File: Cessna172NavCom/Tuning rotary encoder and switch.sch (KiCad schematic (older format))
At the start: 7 parts, among them J3 EN11-HSM1BF20

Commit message: Mostly laid out
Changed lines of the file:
@@
 $Descr A4 11693 8268
 encoding utf-8
-Sheet 6 8
+Sheet 7 15
 Title ""
 Date ""
@@
 AR Path="/5F5DD336/5F5D9328" Ref="R9"  Part="1"
 AR Path="/5F5E0D77/5F5D9328" Ref="R13"  Part="1"
-F 0 "R9" V 5450 3850 50  0000 C CNN
+AR Path="/5F71BCE0/5F5D9328" Ref="R21"  Part="1"
+AR Path="/5F71BCEB/5F5D9328" Ref="R25"  Part="1"
+AR Path="/5F71BCF7/5F5D9328" Ref="R29"  Part="1"
+F 0 "R13" V 5450 3850 50  0000 C CNN
 F 1 "10k" V 5350 3850 50  0000 C CNN
 F 2 "Resistor_SMD:R_0805_2012Metric_Pad1.15x1.40mm_HandSolder" V 5180 3850 50  0001 C CNN
@@
 AR Path="/5F5DD336/5F5D932E" Ref="R10"  Part="1"
 AR Path="/5F5E0D77/5F5D932E" Ref="R14"  Part="1"
-F 0 "R10" V 5350 4050 50  0000 C CNN
+AR Path="/5F71BCE0/5F5D932E" Ref="R22"  Part="1"
+AR Path="/5F71BCEB/5F5D932E" Ref="R26"  Part="1"
+AR Path="/5F71BCF7/5F5D932E" Ref="R30"  Part="1"
+F 0 "R14" V 5350 4050 50  0000 C CNN
 F 1 "10k" V 5450 4050 50  0000 C CNN
 F 2 "Resistor_SMD:R_0805_2012Metric_Pad1.15x1.40mm_HandSolder" V 5180 4050 50  0001 C CNN
@@
 AR Path="/5F5DD336/5F5D9337" Ref="C9"  Part="1"
 AR Path="/5F5E0D77/5F5D9337" Ref="C11"  Part="1"
-F 0 "C9" V 6150 4750 50  0000 C CNN
+AR Path="/5F71BCE0/5F5D9337" Ref="C17"  Part="1"
+AR Path="/5F71BCEB/5F5D9337" Ref="C19"  Part="1"
+AR Path="/5F71BCF7/5F5D9337" Ref="C21"  Part="1"
+F 0 "C11" V 6150 4750 50  0000 C CNN
 F 1 "0.1uf" V 5850 4750 50  0000 C CNN
 F 2 "Capacitor_SMD:C_0805_2012Metric_Pad1.15x1.40mm_HandSolder" H 6038 4600 50  0001 C CNN
@@
 AR Path="/5F5DD336/5F5D933D" Ref="C8"  Part="1"
 AR Path="/5F5E0D77/5F5D933D" Ref="C10"  Part="1"
-F 0 "C8" V 5850 3050 50  0000 L CNN
+AR Path="/5F71BCE0/5F5D933D" Ref="C16"  Part="1"
+AR Path="/5F71BCEB/5F5D933D" Ref="C18"  Part="1"
+AR Path="/5F71BCF7/5F5D933D" Ref="C20"  Part="1"
+F 0 "C10" V 5850 3050 50  0000 L CNN
 F 1 "0.1uf" V 6150 3000 50  0000 L CNN
 F 2 "Capacitor_SMD:C_0805_2012Metric_Pad1.15x1.40mm_HandSolder" H 6038 2950 50  0001 C CNN
@@
 AR Path="/5F5DD336/5F5D934C" Ref="R12"  Part="1"
 AR Path="/5F5E0D77/5F5D934C" Ref="R16"  Part="1"
-F 0 "R12" H 5670 5046 50  0000 L CNN
+AR Path="/5F71BCE0/5F5D934C" Ref="R24"  Part="1"
+AR Path="/5F71BCEB/5F5D934C" Ref="R28"  Part="1"
+AR Path="/5F71BCF7/5F5D934C" Ref="R32"  Part="1"
+F 0 "R16" H 5670 5046 50  0000 L CNN
 F 1 "10k" H 5670 4955 50  0000 L CNN
 F 2 "Resistor_SMD:R_0805_2012Metric_Pad1.15x1.40mm_HandSolder" V 5530 5000 50  0001 C CNN
@@
 AR Path="/5F5DD336/5F5D935D" Ref="R11"  Part="1"
 AR Path="/5F5E0D77/5F5D935D" Ref="R15"  Part="1"
-F 0 "R11" H 5670 2896 50  0000 L CNN
+AR Path="/5F71BCE0/5F5D935D" Ref="R23"  Part="1"
+AR Path="/5F71BCEB/5F5D935D" Ref="R27"  Part="1"
+AR Path="/5F71BCF7/5F5D935D" Ref="R31"  Part="1"
+F 0 "R15" H 5670 2896 50  0000 L CNN
 F 1 "10k" H 5670 2805 50  0000 L CNN
 F 2 "Resistor_SMD:R_0805_2012Metric_Pad1.15x1.40mm_HandSolder" V 5530 2850 50  0001 C CNN
@@
 AR Path="/5F5DD336/5F66C873" Ref="J4"  Part="1"
 AR Path="/5F5E0D77/5F66C873" Ref="J5"  Part="1"
-F 0 "J4" V 6019 3450 50  0000 C CNN
+AR Path="/5F71BCE0/5F66C873" Ref="J1"  Part="1"
+AR Path="/5F71BCEB/5F66C873" Ref="J6"  Part="1"
+AR Path="/5F71BCF7/5F66C873" Ref="J7"  Part="1"
+F 0 "J5" V 6019 3450 50  0000 C CNN
 F 1 "EN11-HSM1BF20" V 6110 3450 50  0000 C CNN
 F 2 "SamacSys_Parts:EN11HSM1BF20" H 7050 3750 50  0001 L CNN

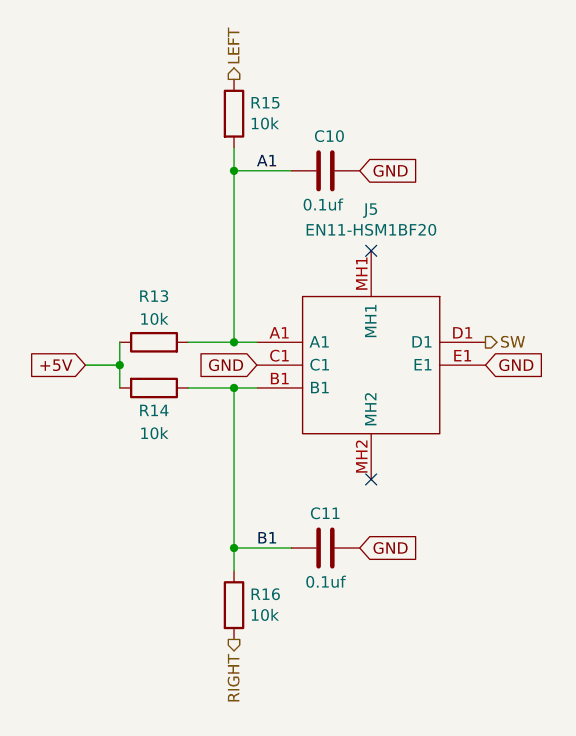
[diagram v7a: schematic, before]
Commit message: Merge connector mapping
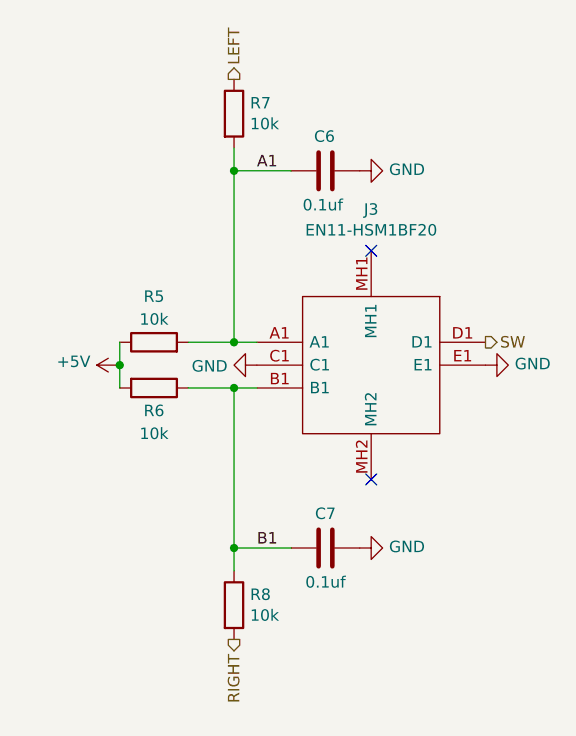
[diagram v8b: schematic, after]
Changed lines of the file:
@@
 $Descr A4 11693 8268
 encoding utf-8
-Sheet 7 15
+Sheet 5 15
 Title ""
 Date ""
@@
 AR Path="/5F71BCEB/5F5D9328" Ref="R25"  Part="1"
 AR Path="/5F71BCF7/5F5D9328" Ref="R29"  Part="1"
-F 0 "R13" V 5450 3850 50  0000 C CNN
+F 0 "R5" V 5450 3850 50  0000 C CNN
 F 1 "10k" V 5350 3850 50  0000 C CNN
 F 2 "Resistor_SMD:R_0805_2012Metric_Pad1.15x1.40mm_HandSolder" V 5180 3850 50  0001 C CNN
@@
 AR Path="/5F71BCEB/5F5D932E" Ref="R26"  Part="1"
 AR Path="/5F71BCF7/5F5D932E" Ref="R30"  Part="1"
-F 0 "R14" V 5350 4050 50  0000 C CNN
+F 0 "R6" V 5350 4050 50  0000 C CNN
 F 1 "10k" V 5450 4050 50  0000 C CNN
 F 2 "Resistor_SMD:R_0805_2012Metric_Pad1.15x1.40mm_HandSolder" V 5180 4050 50  0001 C CNN
@@
 	0    1    1    0
 $EndComp
-Text GLabel 5700 3950 0    50   Input ~ 0
-GND
-Text GLabel 6700 3950 2    50   Input ~ 0
-GND
 $Comp
 L Device:C C?
@@
 AR Path="/5F71BCEB/5F5D9337" Ref="C19"  Part="1"
 AR Path="/5F71BCF7/5F5D9337" Ref="C21"  Part="1"
-F 0 "C11" V 6150 4750 50  0000 C CNN
+F 0 "C7" V 6150 4750 50  0000 C CNN
 F 1 "0.1uf" V 5850 4750 50  0000 C CNN
 F 2 "Capacitor_SMD:C_0805_2012Metric_Pad1.15x1.40mm_HandSolder" H 6038 4600 50  0001 C CNN
@@
 AR Path="/5F71BCEB/5F5D933D" Ref="C18"  Part="1"
 AR Path="/5F71BCF7/5F5D933D" Ref="C20"  Part="1"
-F 0 "C10" V 5850 3050 50  0000 L CNN
+F 0 "C6" V 5850 3050 50  0000 L CNN
 F 1 "0.1uf" V 6150 3000 50  0000 L CNN
 F 2 "Capacitor_SMD:C_0805_2012Metric_Pad1.15x1.40mm_HandSolder" H 6038 2950 50  0001 C CNN
@@
 	0    1    1    0
 $EndComp
-Text GLabel 6150 4750 2    50   Input ~ 0
-GND
-Text GLabel 6150 3100 2    50   Input ~ 0
-GND
 Wire Wire Line
 	5400 3850 5600 3850
-Text GLabel 4950 3950 0    50   Input ~ 0
-+5V
-Wire Wire Line
-	5100 3850 5100 3950
-Wire Wire Line
-	4950 3950 5100 3950
-Connection ~ 5100 3950
-Wire Wire Line
-	5100 3950 5100 4050
 Wire Wire Line
 	5400 4050 5600 4050
@@
 AR Path="/5F71BCEB/5F5D934C" Ref="R28"  Part="1"
 AR Path="/5F71BCF7/5F5D934C" Ref="R32"  Part="1"
-F 0 "R16" H 5670 5046 50  0000 L CNN
+F 0 "R8" H 5670 5046 50  0000 L CNN
 F 1 "10k" H 5670 4955 50  0000 L CNN
 F 2 "Resistor_SMD:R_0805_2012Metric_Pad1.15x1.40mm_HandSolder" V 5530 5000 50  0001 C CNN
@@
 AR Path="/5F71BCEB/5F5D935D" Ref="R27"  Part="1"
 AR Path="/5F71BCF7/5F5D935D" Ref="R31"  Part="1"
-F 0 "R15" H 5670 2896 50  0000 L CNN
+F 0 "R7" H 5670 2896 50  0000 L CNN
 F 1 "10k" H 5670 2805 50  0000 L CNN
 F 2 "Resistor_SMD:R_0805_2012Metric_Pad1.15x1.40mm_HandSolder" V 5530 2850 50  0001 C CNN
@@
 AR Path="/5F71BCEB/5F66C873" Ref="J6"  Part="1"
 AR Path="/5F71BCF7/5F66C873" Ref="J7"  Part="1"
-F 0 "J5" V 6019 3450 50  0000 C CNN
+F 0 "J3" V 6019 3450 50  0000 C CNN
 F 1 "EN11-HSM1BF20" V 6110 3450 50  0000 C CNN
 F 2 "SamacSys_Parts:EN11HSM1BF20" H 7050 3750 50  0001 L CNN
@@
 Text Label 5700 3100 0    50   ~ 0
 A1
+$Comp
+L power:GND #PWR0127
+U 1 1 5F694C04
+P 6150 3100
+AR Path="/5F5D6B2B/5F694C04" Ref="#PWR0127"  Part="1"
+AR Path="/5F5DD336/5F694C04" Ref="#PWR0132"  Part="1"
+AR Path="/5F5E0D77/5F694C04" Ref="#PWR0137"  Part="1"
+AR Path="/5F71BCE0/5F694C04" Ref="#PWR0152"  Part="1"
+AR Path="/5F71BCEB/5F694C04" Ref="#PWR0157"  Part="1"
+AR Path="/5F71BCF7/5F694C04" Ref="#PWR0162"  Part="1"
+F 0 "#PWR0162" H 6150 2850 50  0001 C CNN
+F 1 "GND" V 6155 2972 50  0000 R CNN
+F 2 "" H 6150 3100 50  0001 C CNN
+F 3 "" H 6150 3100 50  0001 C CNN
+	1    6150 3100
+	0    -1   -1   0
+$EndComp
+$Comp
+L power:GND #PWR0128
+U 1 1 5F694D67
+P 6700 3950
+AR Path="/5F5D6B2B/5F694D67" Ref="#PWR0128"  Part="1"
+AR Path="/5F5DD336/5F694D67" Ref="#PWR0133"  Part="1"
+AR Path="/5F5E0D77/5F694D67" Ref="#PWR0138"  Part="1"
+AR Path="/5F71BCE0/5F694D67" Ref="#PWR0153"  Part="1"
+AR Path="/5F71BCEB/5F694D67" Ref="#PWR0158"  Part="1"
+AR Path="/5F71BCF7/5F694D67" Ref="#PWR0163"  Part="1"
+F 0 "#PWR0163" H 6700 3700 50  0001 C CNN
+F 1 "GND" V 6705 3822 50  0000 R CNN
+F 2 "" H 6700 3950 50  0001 C CNN
+F 3 "" H 6700 3950 50  0001 C CNN
+	1    6700 3950
+	0    -1   -1   0
+$EndComp
+$Comp
+L power:GND #PWR0129
+U 1 1 5F694ED6
+P 6150 4750
+AR Path="/5F5D6B2B/5F694ED6" Ref="#PWR0129"  Part="1"
+AR Path="/5F5DD336/5F694ED6" Ref="#PWR0134"  Part="1"
+AR Path="/5F5E0D77/5F694ED6" Ref="#PWR0139"  Part="1"
+AR Path="/5F71BCE0/5F694ED6" Ref="#PWR0154"  Part="1"
+AR Path="/5F71BCEB/5F694ED6" Ref="#PWR0159"  Part="1"
+AR Path="/5F71BCF7/5F694ED6" Ref="#PWR0164"  Part="1"
+F 0 "#PWR0164" H 6150 4500 50  0001 C CNN
+F 1 "GND" V 6155 4622 50  0000 R CNN
+F 2 "" H 6150 4750 50  0001 C CNN
+F 3 "" H 6150 4750 50  0001 C CNN
+	1    6150 4750
+	0    -1   -1   0
+$EndComp
+$Comp
+L power:GND #PWR0130
+U 1 1 5F6951CA
+P 5700 3950
+AR Path="/5F5D6B2B/5F6951CA" Ref="#PWR0130"  Part="1"
+AR Path="/5F5DD336/5F6951CA" Ref="#PWR0135"  Part="1"
+AR Path="/5F5E0D77/5F6951CA" Ref="#PWR0140"  Part="1"
+AR Path="/5F71BCE0/5F6951CA" Ref="#PWR0155"  Part="1"
+AR Path="/5F71BCEB/5F6951CA" Ref="#PWR0160"  Part="1"
+AR Path="/5F71BCF7/5F6951CA" Ref="#PWR0165"  Part="1"
+F 0 "#PWR0165" H 5700 3700 50  0001 C CNN
+F 1 "GND" V 5705 3822 50  0000 R CNN
+F 2 "" H 5700 3950 50  0001 C CNN
+F 3 "" H 5700 3950 50  0001 C CNN
+	1    5700 3950
+	0    1    1    0
+$EndComp
+Wire Wire Line
+	5100 3850 5100 3950
+$Comp
+L power:+5V #PWR0131
+U 1 1 5F695357
+P 5100 3950
+AR Path="/5F5D6B2B/5F695357" Ref="#PWR0131"  Part="1"
+AR Path="/5F5DD336/5F695357" Ref="#PWR0136"  Part="1"
+AR Path="/5F5E0D77/5F695357" Ref="#PWR0141"  Part="1"
+AR Path="/5F71BCE0/5F695357" Ref="#PWR0156"  Part="1"
+AR Path="/5F71BCEB/5F695357" Ref="#PWR0161"  Part="1"
+AR Path="/5F71BCF7/5F695357" Ref="#PWR0166"  Part="1"
+F 0 "#PWR0166" H 5100 3800 50  0001 C CNN
+F 1 "+5V" V 5115 4078 50  0000 L CNN
+F 2 "" H 5100 3950 50  0001 C CNN
+F 3 "" H 5100 3950 50  0001 C CNN
+	1    5100 3950
+	0    -1   -1   0
+$EndComp
+Connection ~ 5100 3950
+Wire Wire Line
+	5100 3950 5100 4050
 $EndSCHEMATC
